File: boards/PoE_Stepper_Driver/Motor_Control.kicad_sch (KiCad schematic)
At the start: 21 parts, among them J2 Motor, J3 Limits, U15 TMC429-I, U16 TMC2660C-PA

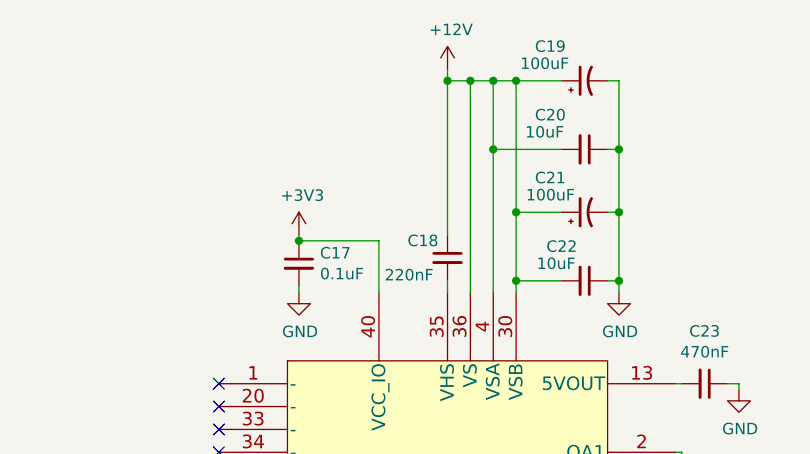
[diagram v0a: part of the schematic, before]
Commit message: motor control draft 1 done, remember to add capacitor C2 and be mindful of adding connection to power
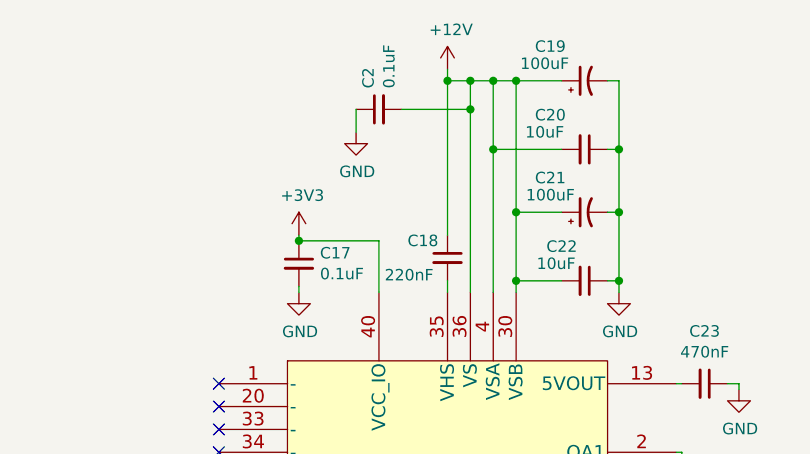
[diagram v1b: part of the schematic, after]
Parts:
- added C2: 0.1uF, Capacitor_SMD:C_0805_2012Metric_Pad1.15x1.40mm_HandSolder, symbol device:C_Small
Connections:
- net +12V: now also C2.2
- net GND: now also C2.1
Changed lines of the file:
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@@
   (junction (at 241.935 85.09) (diameter 0) (color 0 0 0 0)
+  )
+  (junction (at 218.44 44.45) (diameter 0) (color 0 0 0 0)
   )
   (junction (at 49.53 90.17) (diameter 0) (color 0 0 0 0)
@@
     (stroke (width 0) (type default) (color 0 0 0 0))
   )
+  (wire (pts (xy 210.82 44.45) (xy 218.44 44.45))
+    (stroke (width 0) (type default) (color 0 0 0 0))
+  )
   (wire (pts (xy 34.925 95.25) (xy 38.1 95.25))
     (stroke (width 0) (type default) (color 0 0 0 0))
@@
     (stroke (width 0) (type default) (color 0 0 0 0))
   )
+  (wire (pts (xy 205.74 44.45) (xy 205.74 46.99))
+    (stroke (width 0) (type default) (color 0 0 0 0))
+  )
   (wire (pts (xy 173.355 101.6) (xy 173.355 102.235))
     (stroke (width 0) (type default) (color 0 0 0 0))
@@
     (stroke (width 0) (type default) (color 0 0 0 0))
   )
-  (wire (pts (xy 218.44 41.275) (xy 218.44 64.77))
+  (wire (pts (xy 218.44 41.275) (xy 218.44 44.45))
     (stroke (width 0) (type default) (color 0 0 0 0))
   )
@@
   )
   (wire (pts (xy 241.3 105.41) (xy 241.935 105.41))
+    (stroke (width 0) (type default) (color 0 0 0 0))
+  )
+  (wire (pts (xy 218.44 44.45) (xy 218.44 64.77))
     (stroke (width 0) (type default) (color 0 0 0 0))
   )
@@
     )
   )
-  (symbol (lib_id "device:C_Small") (at 199.39 61.595 0)
+  (symbol (lib_id "device:C_Small") (at 199.39 61.595 0) (unit 1)
     (in_bom yes) (on_board yes)
     (property "Reference" "C17" (id 0) (at 201.7268 60.4266 0)
@@
     (pin "2")
   )
-  (symbol (lib_id "power:+3V3") (at 199.39 58.42 0)
+  (symbol (lib_id "power:+3V3") (at 199.39 58.42 0) (unit 1)
     (in_bom yes) (on_board yes)
     (property "Reference" "#PWR031" (id 0) (at 199.39 62.23 0)
@@
     (pin "1")
   )
-  (symbol (lib_id "power:+3V3") (at 67.31 114.3 0)
+  (symbol (lib_id "power:+3V3") (at 67.31 114.3 0) (unit 1)
     (in_bom yes) (on_board yes)
     (property "Reference" "#PWR025" (id 0) (at 67.31 118.11 0)
@@
     (pin "2")
   )
-  (symbol (lib_id "power:+3V3") (at 49.53 74.93 0)
+  (symbol (lib_id "power:+3V3") (at 49.53 74.93 0) (unit 1)
     (in_bom yes) (on_board yes)
     (property "Reference" "#PWR023" (id 0) (at 49.53 78.74 0)
@@
     (pin "1")
   )
-  (symbol (lib_id "Connector:Conn_01x04_Male") (at 29.845 92.71 0) (mirror x)
+  (symbol (lib_id "Connector:Conn_01x04_Male") (at 29.845 92.71 0) (mirror x) (unit 1)
     (in_bom yes) (on_board yes)
     (property "Reference" "J3" (id 0) (at 29.1338 89.7128 0)
@@
     (pin "2")
   )
-  (symbol (lib_id "Connector:Conn_01x04_Male") (at 262.255 100.965 0) (mirror y)
+  (symbol (lib_id "Connector:Conn_01x04_Male") (at 262.255 100.965 0) (mirror y) (unit 1)
     (in_bom yes) (on_board yes)
     (property "Reference" "J2" (id 0) (at 262.9662 103.9622 0)
@@
     (pin "1")
   )
+  (symbol (lib_id "power:GND") (at 205.74 46.99 0) (unit 1)
+    (in_bom yes) (on_board yes)
+    (property "Reference" "#PWR0101" (id 0) (at 205.74 53.34 0)
+      (effects (font (size 1.27 1.27)) hide)
+    )
+    (property "Value" "GND" (id 1) (at 205.867 51.3842 0))
+    (property "Footprint" "" (id 2) (at 205.74 46.99 0)
+      (effects (font (size 1.27 1.27)) hide)
+    )
+    (property "Datasheet" "" (id 3) (at 205.74 46.99 0)
+      (effects (font (size 1.27 1.27)) hide)
+    )
+    (pin "1")
+  )
+  (symbol (lib_id "device:C_Small") (at 208.28 44.45 90) (unit 1)
+    (in_bom yes) (on_board yes)
+    (property "Reference" "C2" (id 0) (at 207.1116 42.1132 0)
+      (effects (font (size 1.27 1.27)) (justify left))
+    )
+    (property "Value" "0.1uF" (id 1) (at 209.423 42.1132 0)
+      (effects (font (size 1.27 1.27)) (justify left))
+    )
+    (property "Footprint" "Capacitor_SMD:C_0805_2012Metric_Pad1.15x1.40mm_HandSolder" (id 2) (at 208.28 44.45 0)
+      (effects (font (size 1.27 1.27)) hide)
+    )
+    (property "Datasheet" "~" (id 3) (at 208.28 44.45 0)
+      (effects (font (size 1.27 1.27)) hide)
+    )
+    (pin "1")
+    (pin "2")
+  )
 )
